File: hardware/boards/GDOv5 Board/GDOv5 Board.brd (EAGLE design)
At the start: 34 x 78.7 mm, 29 parts, among them IC1 DS1820, IC2 3.3V REG, J1 DCJ0202

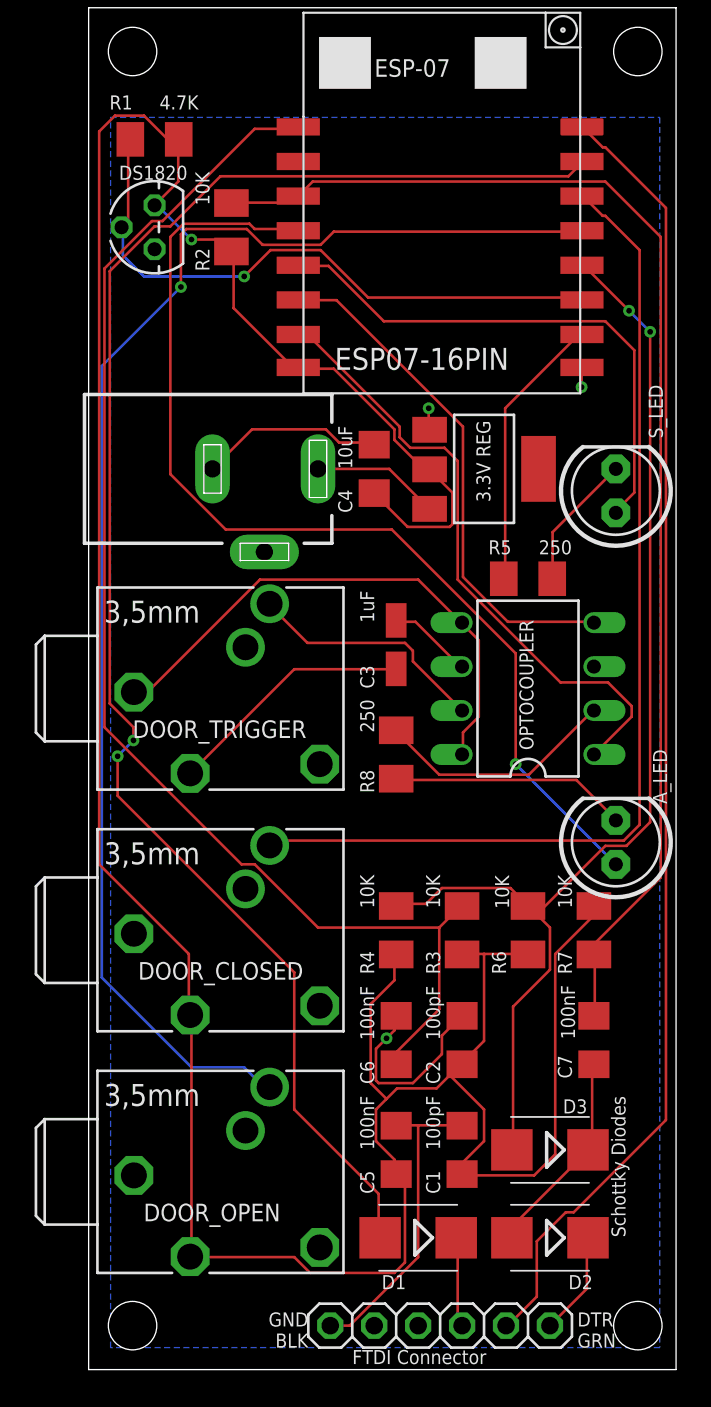
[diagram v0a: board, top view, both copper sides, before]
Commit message: Added resistor for optocoupler inputs
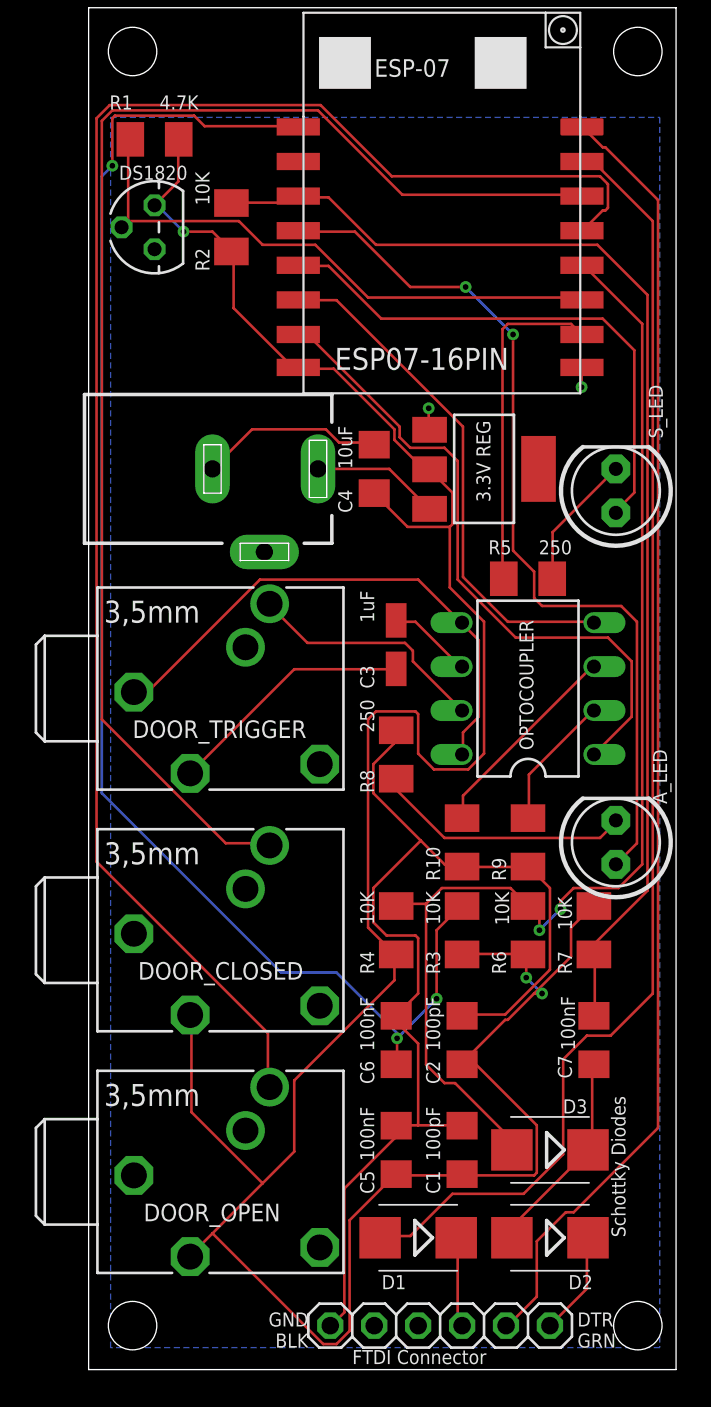
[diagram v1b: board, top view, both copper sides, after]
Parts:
- added R10, R9: 50, resistor:M3216
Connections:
- new net N$6: CTRL_OUT.2, R9.2
- new net N$7: CTRL_OUT.3, R10.2
- net GND: now also R10.1, R9.1; no longer CTRL_OUT.2, CTRL_OUT.3
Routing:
- net GND: track 56.8 -> 78.4 mm, vias 3 -> 2
- net +3.3V: track 188.7 -> 167.7 mm, vias 1 -> 3
- net RXD: track 93.1 -> 75.0 mm, vias 2 -> 0
- net ARD04: track 59.8 -> 77.4 mm
- net ARD05: track 81.2 -> 95.3 mm, vias 1 -> 0
- net N$7: track 0.00 -> 12.0 mm
- net ARD16: track 60.4 -> 51.7 mm, vias 1 -> 2
- net RESET: track 76.0 -> 84.1 mm, vias 0 -> 3
- net N$6: track 0.00 -> 7.81 mm
- net ENABLE: track 73.3 -> 69.6 mm
- net ARD0_FLASH: track 67.4 -> 70.8 mm
- net ARD15: track 16.2 -> 19.4 mm
- net ARD02: track 35.9 -> 34.1 mm, vias 1 -> 0
- net ARD13: track 36.3 -> 37.8 mm
- net N$5: track 13.7 -> 15.0 mm

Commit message: More board tweaks
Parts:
- removed C5: 100nF, resistor:C1206
- added C8, C9: 10uF, SparkFun-Capacitors:EIA3216
- C3: device rcl:CT3216 -> SparkFun-Capacitors:1206
- C4: value 10uF -> 100nF
- D1, D2, D3: device diode:SMB -> adafruit:SOD-123
- moved C4 15.3 mm to (17.8, 38.1)
- moved C3 10.2 mm to (16.5, 53.3)
- moved D1 9.16 mm to (26.7, 14.0)
- moved D3 6.35 mm to (26.7, 7.62), turned to 0 degrees
- moved C1 6.35 mm to (25.4, 19.1)
- moved R2 5.68 mm to (5.71, 62.2), turned to 0 degrees
- moved R8 5.08 mm to (17.8, 31.8)
- moved R6 4.02 mm to (29.2, 25.4)
- moved R7 4.02 mm to (25.4, 25.4)
- moved JP1 3.19 mm to (17.1, 4.13)
- moved D2 2.54 mm to (26.7, 11.4)
- moved R1 1.90 mm to (5.71, 72.4)
- moved R3 1.27 mm to (21.6, 25.4)
- moved R4 1.27 mm to (17.8, 25.4)
- moved R5 1.27 mm to (26.7, 47.0)
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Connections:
- net +3.3V: now also C9.A; no longer C5.1
- net +5V: now also C8.A
- net GND: now also C8.C, C9.C; no longer C5.2
- net LIGHTS+: now also C3.2; no longer C3.+
- net N$3: now also C3.1; no longer C3.-
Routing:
- net +3.3V: track 167.7 -> 0.00 mm, vias 3 -> 0
- net ARD05: track 95.3 -> 0.00 mm
- net RESET: track 84.1 -> 0.00 mm, vias 3 -> 0
- net GND: track 78.4 -> 0.00 mm, vias 2 -> 0
- net ARD04: track 77.4 -> 0.00 mm
- net TXD: track 75.2 -> 0.00 mm
- net RXD: track 75.0 -> 0.00 mm
- net ARD0_FLASH: track 70.8 -> 0.00 mm, vias 2 -> 0
- net ENABLE: track 69.6 -> 0.00 mm
- net ARD16: track 51.7 -> 0.00 mm, vias 2 -> 0
- net ARD13: track 37.8 -> 0.00 mm
- net ARD02: track 34.1 -> 0.00 mm
- net ARD14: track 31.3 -> 0.00 mm
- net CTRL-: track 31.1 -> 0.00 mm
- net ARD12: track 29.9 -> 0.00 mm
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
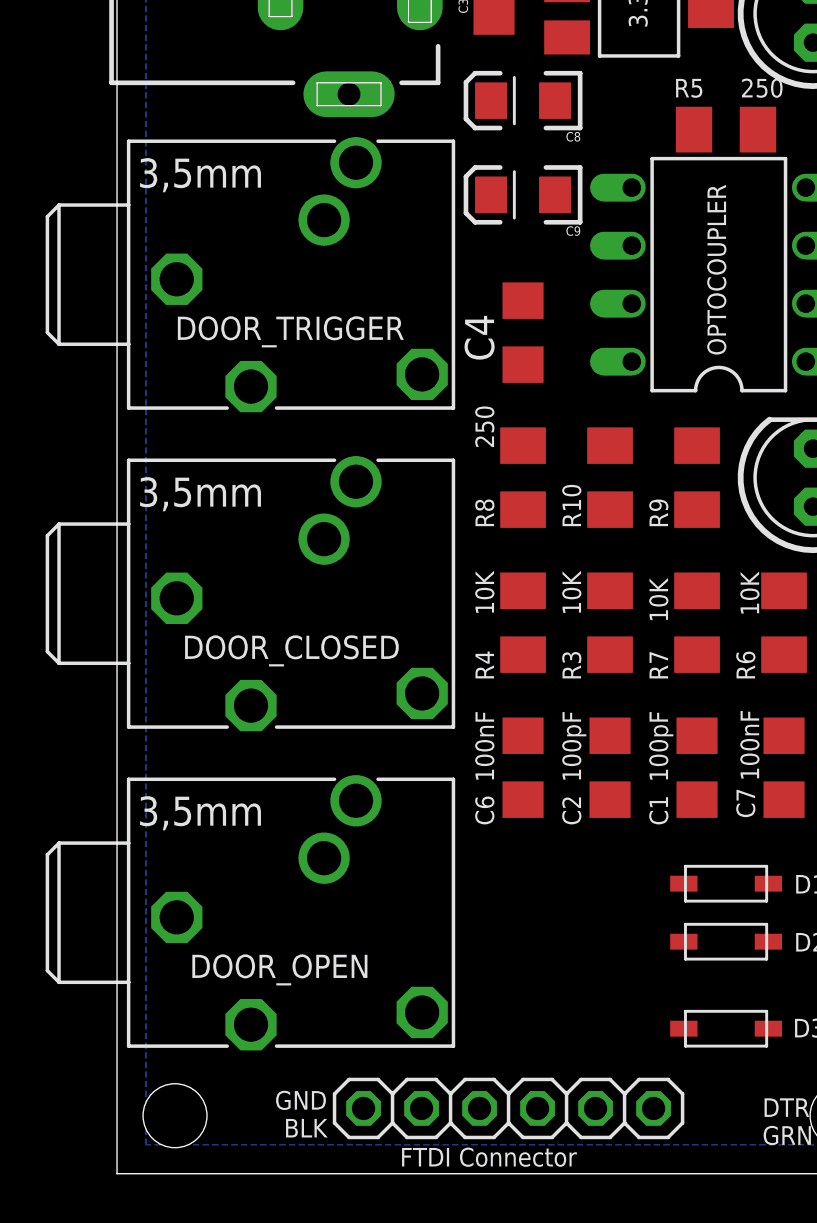
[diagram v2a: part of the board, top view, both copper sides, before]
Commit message: Replacing 3.5mm Jack with SMT design
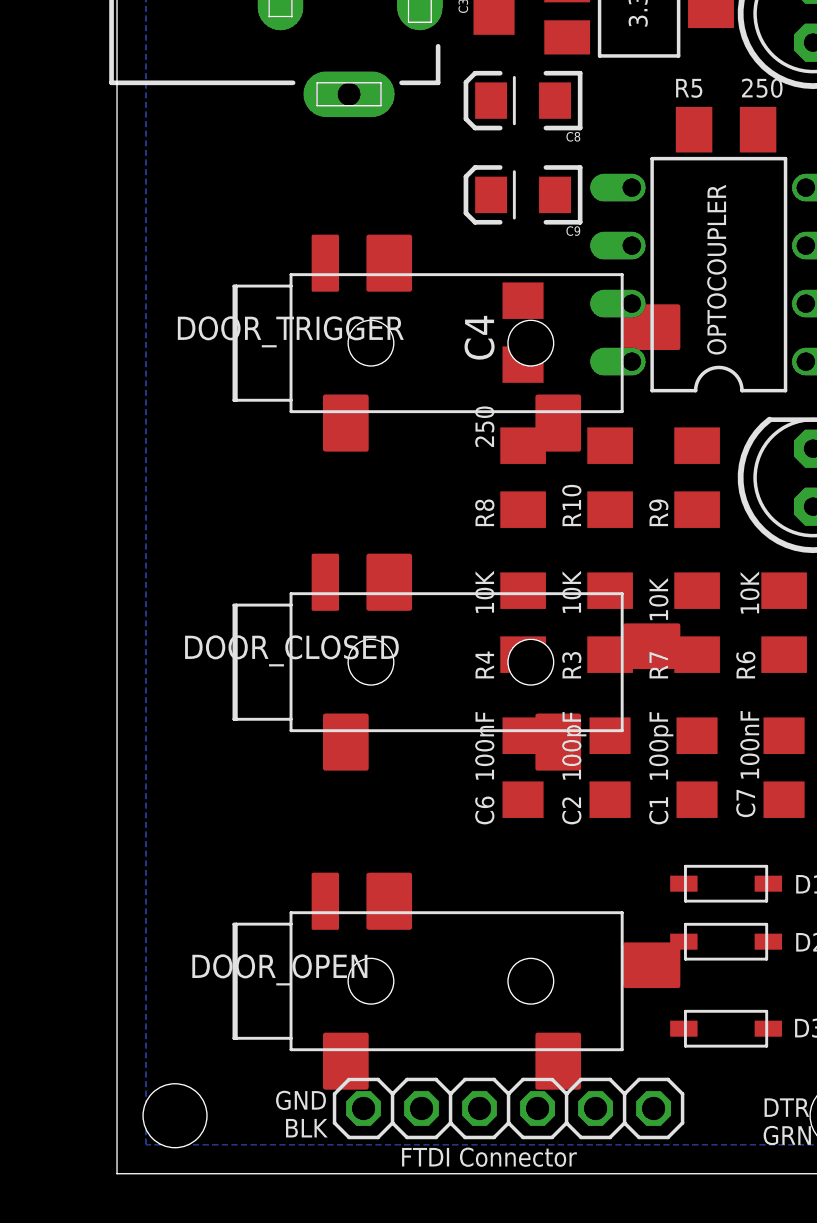
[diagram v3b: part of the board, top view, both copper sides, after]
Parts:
- DOOR_CLOSED, DOOR_OPEN, DOOR_TRIGGER: value PG203J -> PG203JPJ-328; device con-hirschmann:PG203J -> PJ-328 Jack:PG203J
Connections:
- net +3.3V: now also DOOR_CLOSED.TIP, DOOR_OPEN.TIP; no longer DOOR_CLOSED.5, DOOR_OPEN.5
- net ARD04: now also DOOR_CLOSED.RING; no longer DOOR_CLOSED.2
- net ARD05: now also DOOR_OPEN.RING; no longer DOOR_OPEN.2
- net CTRL-: now also DOOR_TRIGGER.GND; no longer DOOR_TRIGGER.1
- net DOOR+: now also DOOR_TRIGGER.RING; no longer DOOR_TRIGGER.2
- net GND: now also DOOR_CLOSED.GND, DOOR_OPEN.GND; no longer DOOR_CLOSED.1, DOOR_OPEN.1
- net LIGHTS+: now also DOOR_TRIGGER.TIP; no longer DOOR_TRIGGER.5
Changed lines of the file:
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@@
 <attribute name="VALUE" x="24.511" y="4.191" size="1.27" layer="27"/>
 </element>
-<element name="DOOR_CLOSED" library="con-hirschmann" package="PG203J" value="PG203J" x="7.62" y="26.67" smashed="yes">
-<attribute name="MPN" value="" x="7.62" y="26.67" size="1.778" layer="27" display="off"/>
-<attribute name="MF" value="" x="7.62" y="26.67" size="1.778" layer="27" display="off"/>
-<attribute name="OC_FARNELL" value="unknown" x="7.62" y="26.67" size="1.778" layer="27" display="off"/>
-<attribute name="OC_NEWARK" value="unknown" x="7.62" y="26.67" size="1.778" layer="27" display="off"/>
+<element name="DOOR_CLOSED" library="PJ-328 Jack" package="PG203J" value="PG203JPJ-328" x="7.62" y="26.67" smashed="yes">
 <attribute name="NAME" x="2.8575" y="23.8125" size="1.016" layer="25" ratio="10"/>
 </element>
-<element name="DOOR_TRIGGER" library="con-hirschmann" package="PG203J" value="PG203J" x="7.62" y="40.64" smashed="yes">
-<attribute name="MPN" value="" x="7.62" y="40.64" size="1.778" layer="27" display="off"/>
-<attribute name="MF" value="" x="7.62" y="40.64" size="1.778" layer="27" display="off"/>
-<attribute name="OC_FARNELL" value="unknown" x="7.62" y="40.64" size="1.778" layer="27" display="off"/>
-<attribute name="OC_NEWARK" value="unknown" x="7.62" y="40.64" size="1.778" layer="27" display="off"/>
+<element name="DOOR_TRIGGER" library="PJ-328 Jack" package="PG203J" value="PG203JPJ-328" x="7.62" y="40.64" smashed="yes">
 <attribute name="NAME" x="2.54" y="37.7825" size="1.016" layer="25" ratio="10" rot="R180" align="top-right"/>
 </element>
-<element name="DOOR_OPEN" library="con-hirschmann" package="PG203J" value="PG203J" x="7.62" y="12.7" smashed="yes">
-<attribute name="MPN" value="" x="7.62" y="12.7" size="1.778" layer="27" display="off"/>
-<attribute name="MF" value="" x="7.62" y="12.7" size="1.778" layer="27" display="off"/>
-<attribute name="OC_FARNELL" value="unknown" x="7.62" y="12.7" size="1.778" layer="27" display="off"/>
-<attribute name="OC_NEWARK" value="unknown" x="7.62" y="12.7" size="1.778" layer="27" display="off"/>
+<element name="DOOR_OPEN" library="PJ-328 Jack" package="PG203J" value="PG203JPJ-328" x="7.62" y="12.7" smashed="yes">
 <attribute name="NAME" x="3.175" y="9.8425" size="1.016" layer="25" ratio="10" rot="R180" align="top-right"/>
 </element>
@@
 <contactref element="J1" pad="3"/>
 <contactref element="IC2" pad="1"/>
-<contactref element="DOOR_CLOSED" pad="1"/>
+<contactref element="DOOR_CLOSED" pad="GND"/>
 <contactref element="C1" pad="2"/>
-<contactref element="DOOR_OPEN" pad="1"/>
+<contactref element="DOOR_OPEN" pad="GND"/>
 <contactref element="C2" pad="2"/>
 <contactref element="U$1" pad="GND"/>
@@
 <signal name="+3.3V">
 <contactref element="IC2" pad="2"/>
-<contactref element="DOOR_OPEN" pad="5"/>
+<contactref element="DOOR_OPEN" pad="TIP"/>
 <contactref element="C2" pad="1"/>
-<contactref element="DOOR_CLOSED" pad="5"/>
+<contactref element="DOOR_CLOSED" pad="TIP"/>
 <contactref element="C1" pad="1"/>
 <contactref element="U$1" pad="VCC"/>
@@
 <wire x1="21.59" y1="17.65" x2="21.59" y2="24" width="0" layer="19" extent="1-1"/>
 <wire x1="25.4" y1="17.65" x2="21.59" y2="17.65" width="0" layer="19" extent="1-1"/>
-<wire x1="5.8674" y1="21.7678" x2="17.78" y2="24" width="0" layer="19" extent="1-1"/>
-<wire x1="5.8674" y1="7.7978" x2="5.8674" y2="21.7678" width="0" layer="19" extent="1-1"/>
+<wire x1="19.32" y1="20.17" x2="17.78" y2="24" width="0" layer="19" extent="1-1"/>
+<wire x1="19.32" y1="6.2" x2="19.32" y2="20.17" width="0" layer="19" extent="1-1"/>
 </signal>
 <signal name="ARD05">
-<contactref element="DOOR_OPEN" pad="2"/>
+<contactref element="DOOR_OPEN" pad="RING"/>
 <contactref element="U$1" pad="GPIO5"/>
-<wire x1="10.4648" y1="17.6022" x2="28.52" y2="67.11" width="0" layer="19" extent="1-1"/>
+<wire x1="11.92" y1="13.2" x2="28.52" y2="67.11" width="0" layer="19" extent="1-1"/>
 </signal>
 <signal name="ARD04">
-<contactref element="DOOR_CLOSED" pad="2"/>
+<contactref element="DOOR_CLOSED" pad="RING"/>
 <contactref element="U$1" pad="GPIO4"/>
-<wire x1="10.4648" y1="31.5722" x2="28.52" y2="69.11" width="0" layer="19" extent="1-1"/>
+<wire x1="11.92" y1="27.17" x2="28.52" y2="69.11" width="0" layer="19" extent="1-1"/>
 </signal>
 <signal name="DOOR+">
 <contactref element="CTRL_OUT" pad="7"/>
-<contactref element="DOOR_TRIGGER" pad="2"/>
-<wire x1="10.4648" y1="45.5422" x2="22.5425" y2="39.37" width="0" layer="19" extent="1-1"/>
+<contactref element="DOOR_TRIGGER" pad="RING"/>
+<wire x1="11.92" y1="41.14" x2="22.5425" y2="39.37" width="0" layer="19" extent="1-1"/>
 </signal>
 <signal name="CTRL-">
 <contactref element="CTRL_OUT" pad="8"/>
 <contactref element="CTRL_OUT" pad="5"/>
-<contactref element="DOOR_TRIGGER" pad="1"/>
+<contactref element="DOOR_TRIGGER" pad="GND"/>
 <wire x1="22.5425" y1="36.83" x2="22.5425" y2="44.45" width="0" layer="19" extent="1-1"/>
-<wire x1="2.6162" y1="40.4368" x2="22.5425" y2="36.83" width="0" layer="19" extent="1-1"/>
+<wire x1="10.02" y1="34.14" x2="22.5425" y2="36.83" width="0" layer="19" extent="1-1"/>
 </signal>
 <signal name="N$3">
@@
 </signal>
 <signal name="LIGHTS+">
-<contactref element="DOOR_TRIGGER" pad="5"/>
+<contactref element="DOOR_TRIGGER" pad="TIP"/>
 <contactref element="C3" pad="2"/>
-<wire x1="5.8674" y1="35.7378" x2="16.51" y2="54.74" width="0" layer="19" extent="1-1"/>
+<wire x1="19.32" y1="34.14" x2="16.51" y2="54.74" width="0" layer="19" extent="1-1"/>
 </signal>
 <signal name="ARD12">
